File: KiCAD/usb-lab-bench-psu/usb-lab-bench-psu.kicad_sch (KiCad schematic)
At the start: 11 parts, among them J2 USB_C_Receptacle, J5 Conn_02x02_Top_Bottom, SW2 SW_Push, U6 USBLC6-2SC6

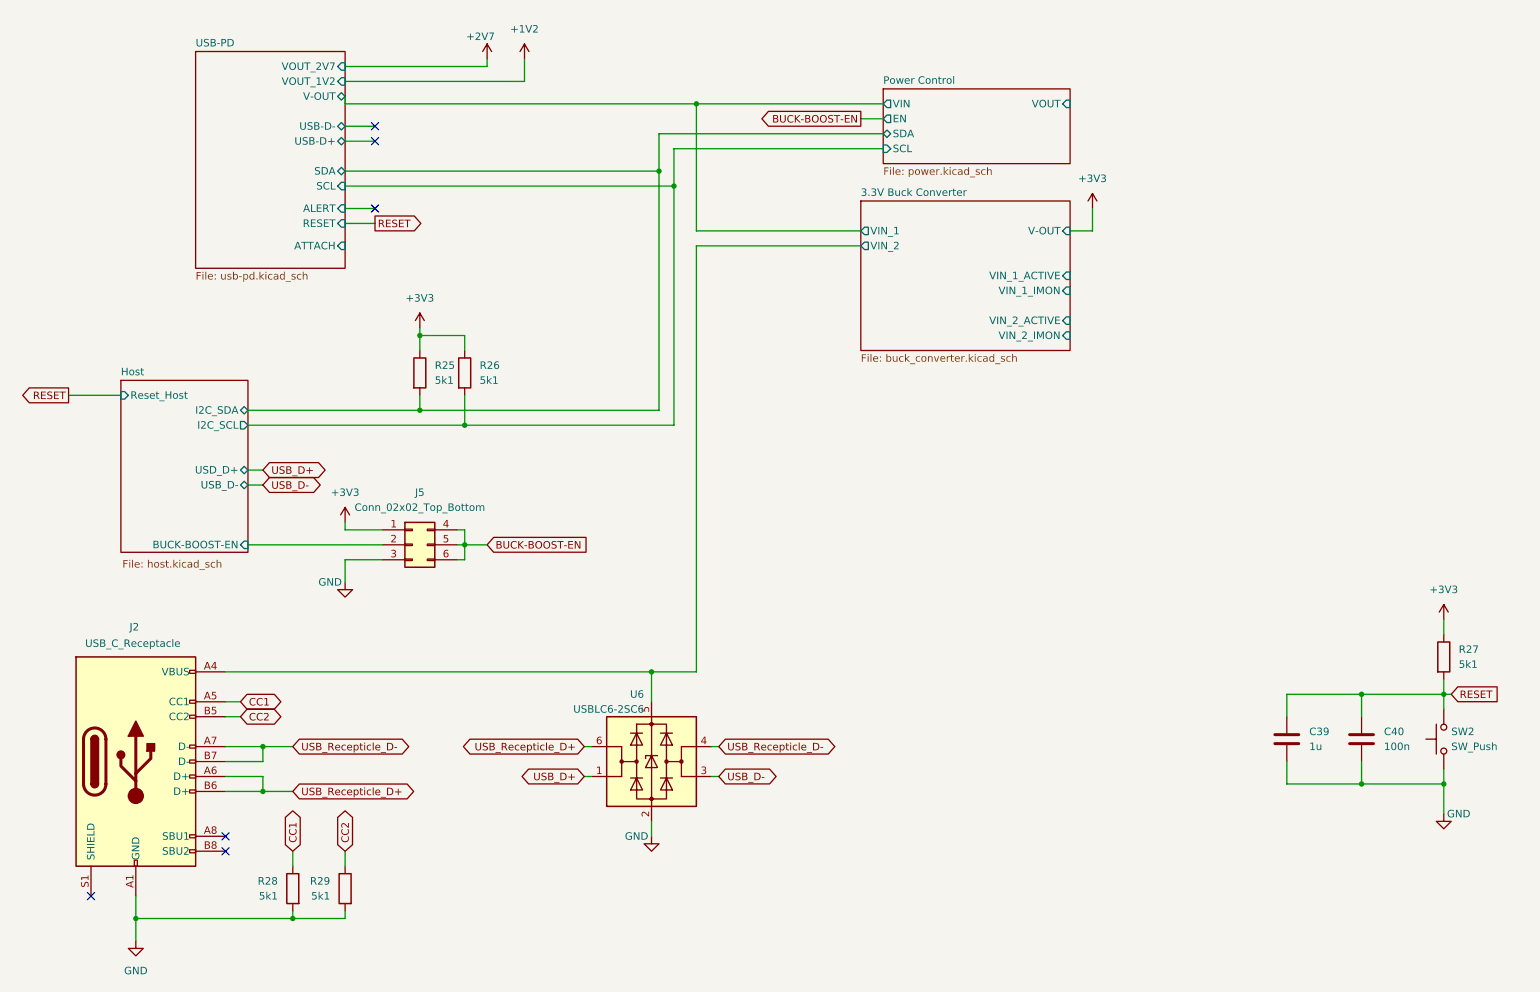
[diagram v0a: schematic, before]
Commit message: Replaced global labels with labels, added measurement circuit, started with io board
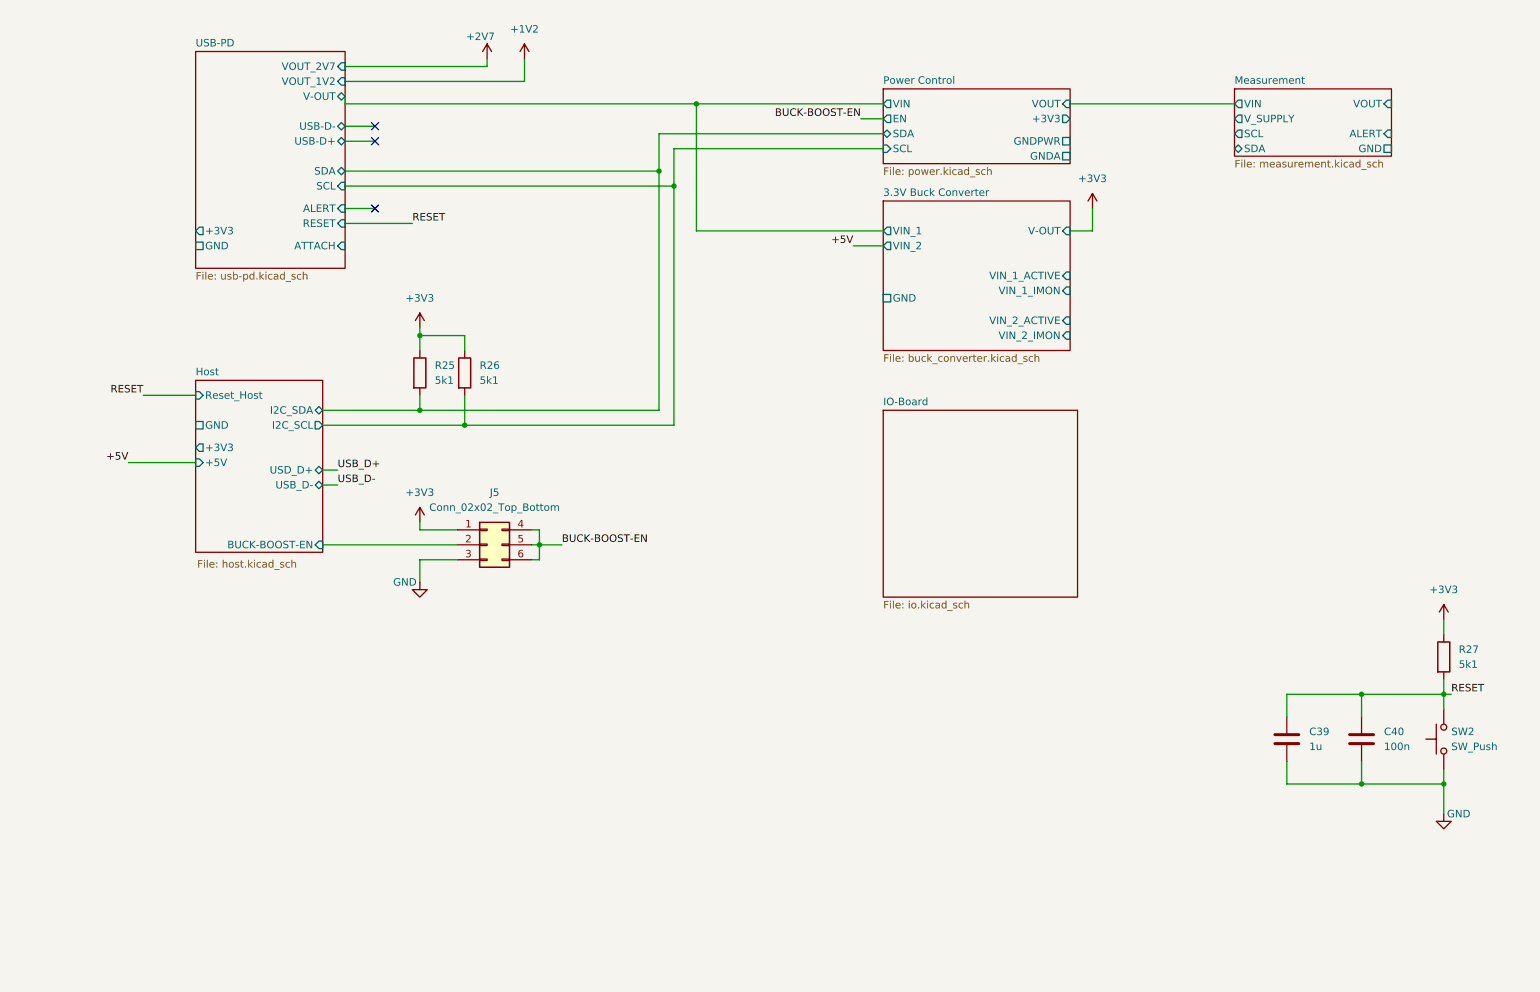
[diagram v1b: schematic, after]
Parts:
- removed J2: USB_C_Receptacle, Prj_Connectors_USB:USB_C_Receptacle_SHOU_HAN_TYPE_C_16P_CB1.6_073, symbol Connector:USB_C_Receptacle_USB2.0
- removed R28, R29: 5k1, Resistor_SMD:R_0402_1005Metric_Pad0.72x0.64mm_HandSolder, symbol Device:R
- removed U6: USBLC6-2SC6, Package_TO_SOT_SMD:SOT-23-6, symbol Power_Protection:USBLC6-2SC6
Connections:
- no-connect marks 6 -> 3
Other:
- added sheet IO-Board (io.kicad_sch)
- added sheet Measurement (measurement.kicad_sch)
- sheet 3.3V Buck Converter ports: added GND; removed none
- sheet Host ports: added +3V3, +5V, GND; removed none
- sheet Power Control ports: added +3V3, GNDA, GNDPWR; removed none
- sheet USB-PD ports: added +3V3, GND; removed none
- moved on the sheet: J5

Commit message: updated GND and supply nets, switched buck-boost-converter
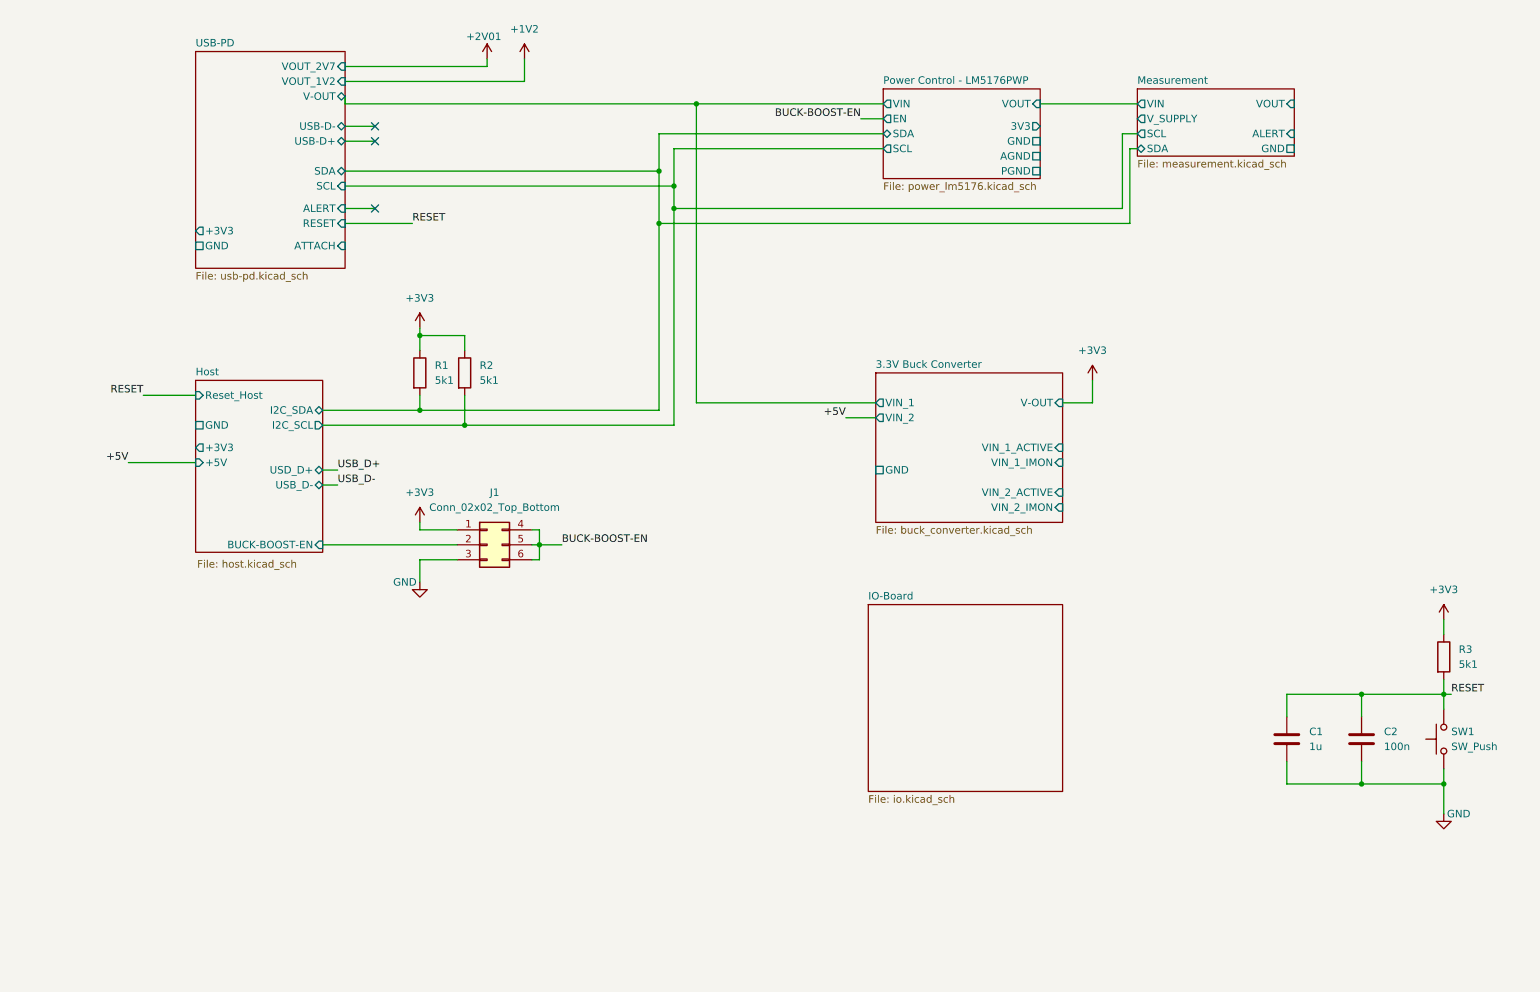
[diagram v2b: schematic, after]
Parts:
- renumbered C39 to C1, C40 to C2, J5 to J1, R25 to R1, R26 to R2, R27 to R3, SW2 to SW1
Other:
- removed sheet Power Control
- added sheet Power Control - LM5176PWP (power_lm5176.kicad_sch)

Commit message: added current limitting feedback circuit
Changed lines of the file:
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@@
 		(on_board no)
 		(dnp no)
-		(property "Reference" "+2V01"
+		(property "Reference" "#+2V01"
 			(at 95.504 24.13 0)
 			(effects
@@
 			(project ""
 				(path "/63928bc9-e618-488a-a687-c6d5597f31d9"
-					(reference "+2V01")
+					(reference "#+2V01")
 					(unit 1)
 				)

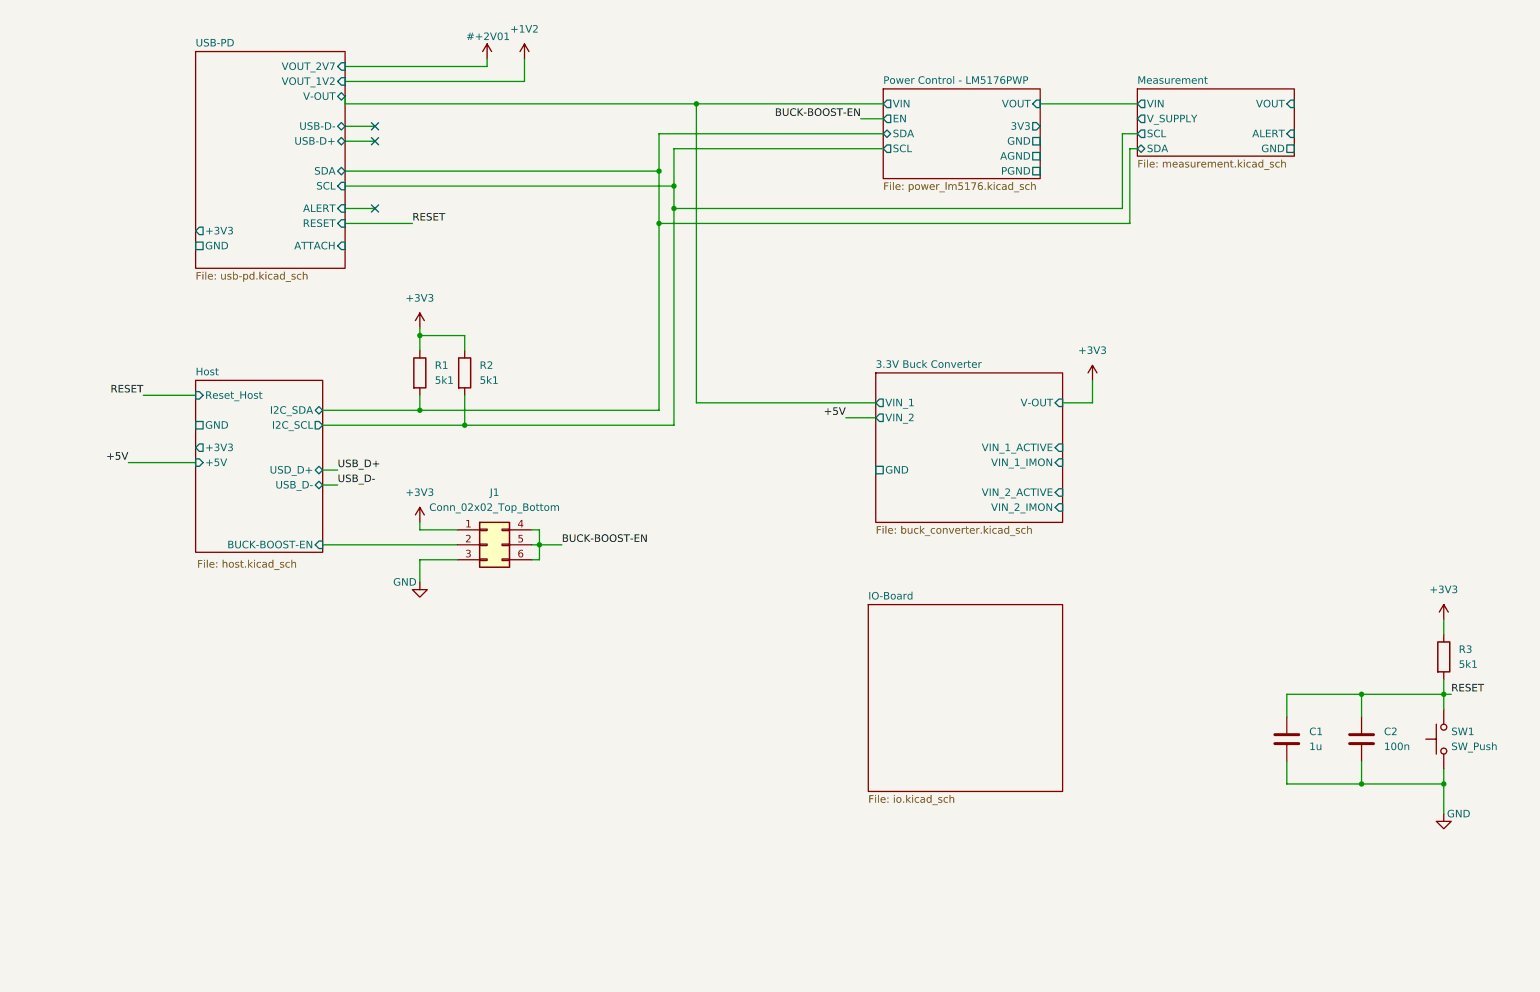
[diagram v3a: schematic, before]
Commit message: adapted buck converter
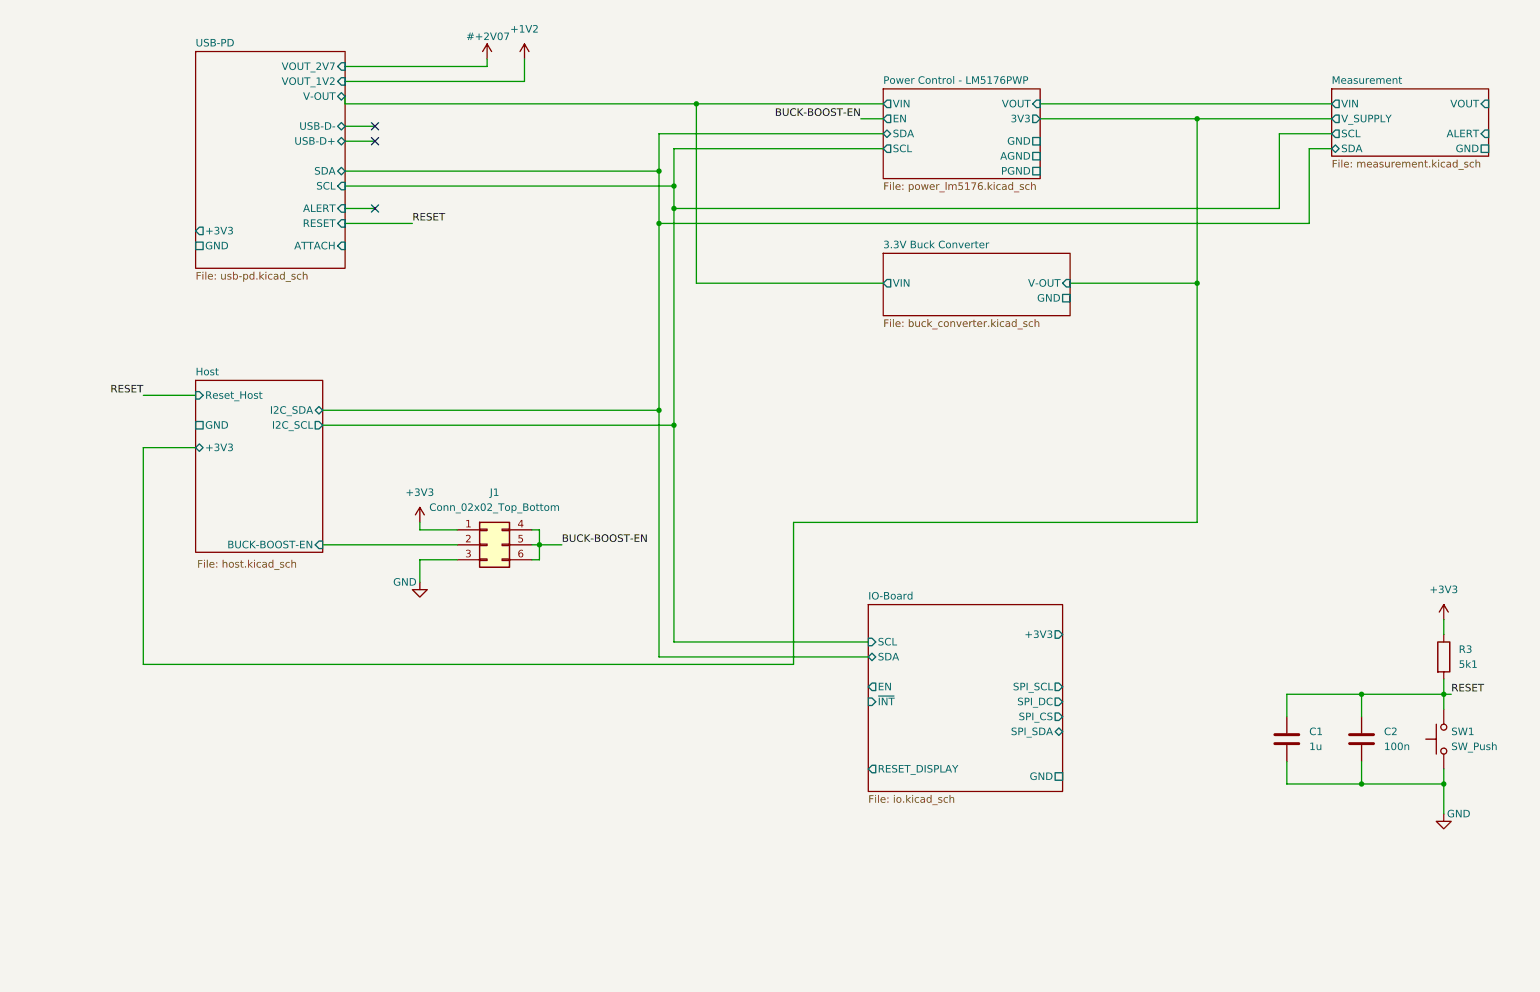
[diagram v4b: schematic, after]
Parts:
- removed R1, R2: 5k1, symbol Device:R
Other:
- sheet 3.3V Buck Converter ports: added VIN; removed VIN_1, VIN_1_ACTIVE, VIN_1_IMON, VIN_2, VIN_2_ACTIVE, VIN_2_IMON
- sheet Host ports: added none; removed +5V, USB_D-, USD_D+
- sheet IO-Board ports: added +3V3, EN, GND, RESET_DISPLAY, SCL, SDA, SPI_CS, SPI_DC, SPI_SCL, SPI_SDA, ~{INT}; removed none
